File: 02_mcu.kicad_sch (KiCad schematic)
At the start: 31 parts, among them J2 0533980571, U3 MSPM0C1104SDDFR, U4 TLC59208F, U5 VEML7700, U6 TLV803E

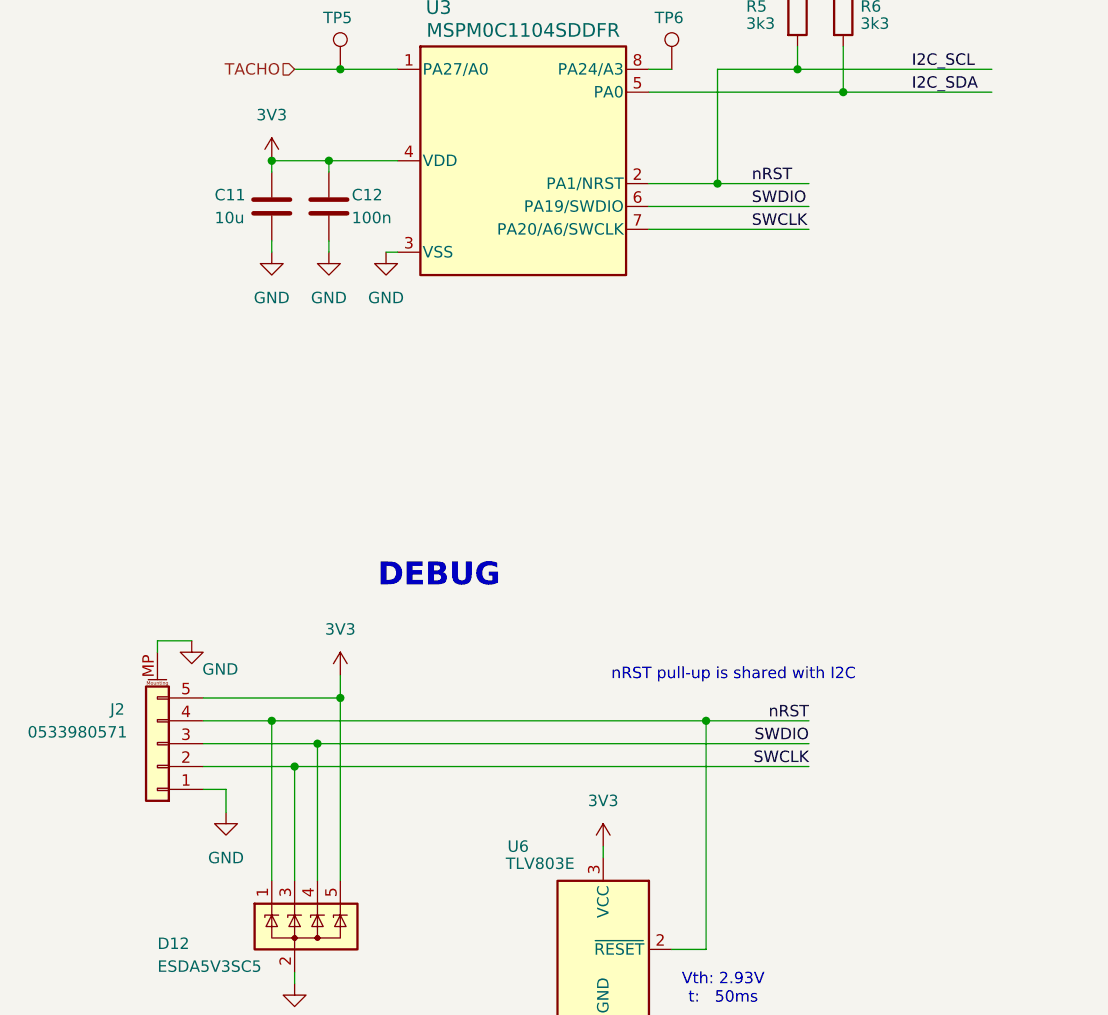
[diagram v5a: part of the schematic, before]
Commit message: Schematic: Remove nRST net label to avoid ERC warning
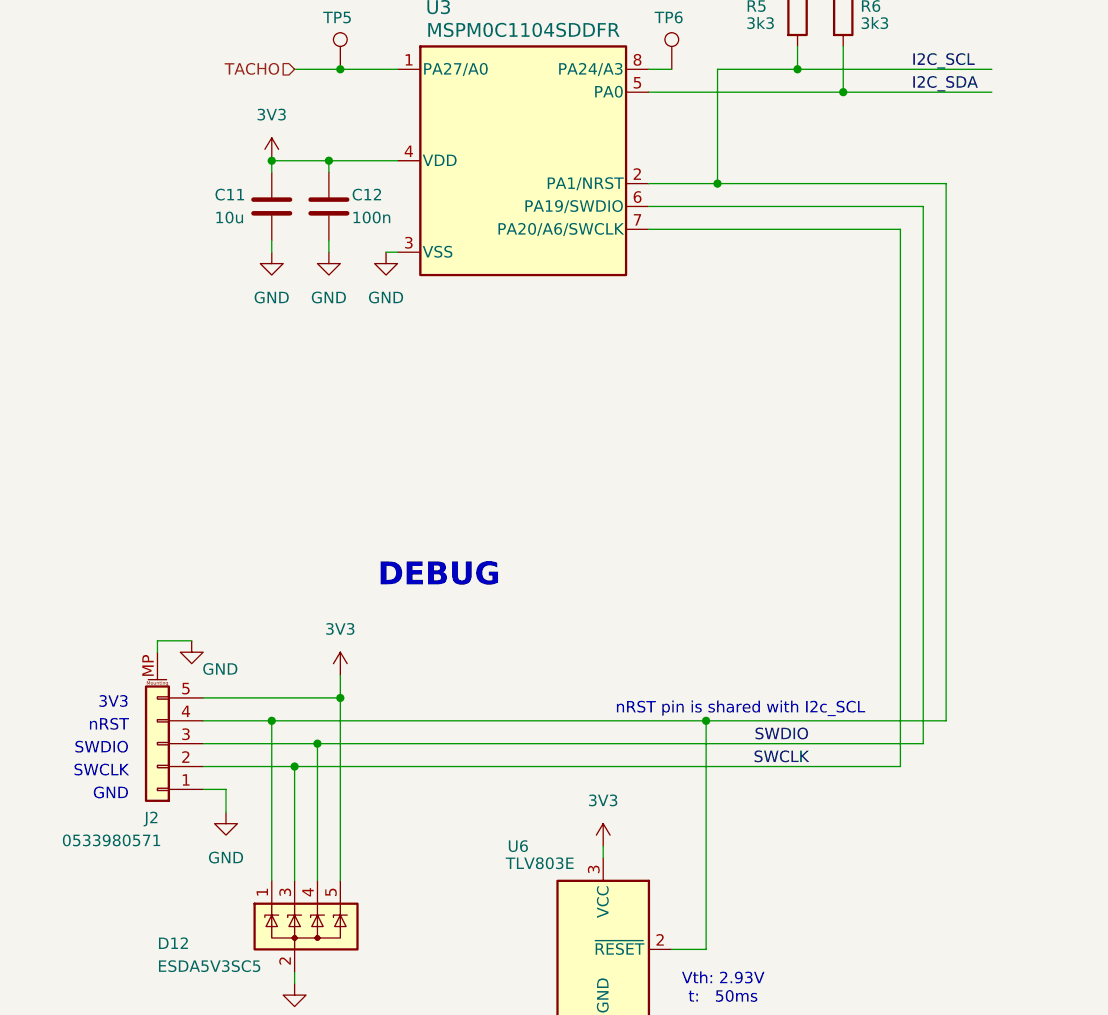
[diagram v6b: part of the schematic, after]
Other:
- note added: "3V3"
- note added: "GND"
- note added: "SWCLK"
- note added: "SWDIO"
- note added: "nRST"
- note added: "nRST pin is shared with I2c_SCL"
- note removed: "nRST pull-up is shared with I2C"
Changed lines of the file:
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@@
 	(wire
 		(pts
-			(xy 50.8 132.08) (xy 105.41 132.08)
+			(xy 50.8 132.08) (xy 118.11 132.08)
 		)
 		(stroke
@@
 	(wire
 		(pts
+			(xy 118.11 72.39) (xy 118.11 132.08)
+		)
+		(stroke
+			(width 0)
+			(type default)
+		)
+	)
+	(wire
+		(pts
 			(xy 213.36 85.09) (xy 213.36 92.71)
 		)
@@
 	(wire
 		(pts
-			(xy 87.63 74.93) (xy 105.41 74.93)
+			(xy 87.63 74.93) (xy 115.57 74.93)
 		)
 		(stroke
@@
 	(wire
 		(pts
-			(xy 48.26 134.62) (xy 105.41 134.62)
+			(xy 48.26 134.62) (xy 115.57 134.62)
 		)
 		(stroke
@@
 	(wire
 		(pts
+			(xy 115.57 74.93) (xy 115.57 134.62)
+		)
+		(stroke
+			(width 0)
+			(type default)
+		)
+	)
+	(wire
+		(pts
 			(xy 87.63 57.15) (xy 90.17 57.15)
 		)
@@
 	(wire
 		(pts
-			(xy 95.25 69.85) (xy 105.41 69.85)
+			(xy 95.25 69.85) (xy 120.65 69.85)
 		)
 		(stroke
@@
 	(wire
 		(pts
-			(xy 93.98 129.54) (xy 105.41 129.54)
+			(xy 93.98 129.54) (xy 120.65 129.54)
 		)
 		(stroke
@@
 	(wire
 		(pts
+			(xy 120.65 69.85) (xy 120.65 129.54)
+		)
+		(stroke
+			(width 0)
+			(type default)
+		)
+	)
+	(wire
+		(pts
 			(xy 181.61 87.63) (xy 181.61 90.17)
 		)
@@
 	(wire
 		(pts
-			(xy 87.63 72.39) (xy 105.41 72.39)
+			(xy 87.63 72.39) (xy 118.11 72.39)
 		)
 		(stroke
@@
 		)
 	)
+	(text "nRST"
+		(exclude_from_sim no)
+		(at 29.845 130.175 0)
+		(effects
+			(font
+				(size 1.27 1.27)
+			)
+			(justify right)
+		)
+	)
 	(text "MCU"
 		(exclude_from_sim no)
@@
 		)
 	)
-	(text "nRST pull-up is shared with I2C"
-		(exclude_from_sim no)
-		(at 97.028 124.46 0)
+	(text "SWCLK"
+		(exclude_from_sim no)
+		(at 29.845 135.255 0)
 		(effects
 			(font
 				(size 1.27 1.27)
 			)
+			(justify right)
+		)
+	)
+	(text "3V3"
+		(exclude_from_sim no)
+		(at 29.845 127.635 0)
+		(effects
+			(font
+				(size 1.27 1.27)
+			)
+			(justify right)
+		)
+	)
+	(text "nRST pin is shared with I2c_SCL"
+		(exclude_from_sim no)
+		(at 97.79 128.27 0)
+		(effects
+			(font
+				(size 1.27 1.27)
+			)
+		)
+	)
+	(text "GND"
+		(exclude_from_sim no)
+		(at 29.845 137.795 0)
+		(effects
+			(font
+				(size 1.27 1.27)
+			)
+			(justify right)
 		)
 	)
@@
 		)
 	)
+	(text "SWDIO"
+		(exclude_from_sim no)
+		(at 29.845 132.715 0)
+		(effects
+			(font
+				(size 1.27 1.27)
+			)
+			(justify right)
+		)
+	)
 	(text "DEBUG"
 		(exclude_from_sim no)
@@
 		)
 	)
-	(label "SWCLK"
-		(at 99.06 74.93 0)
-		(fields_autoplaced yes)
-		(effects
-			(font
-				(size 1.27 1.27)
-			)
-			(justify left bottom)
-		)
-	)
 	(label "I2C_SCL"
 		(at 116.84 57.15 0)
@@
 		)
 	)
-	(label "nRST"
-		(at 99.06 69.85 0)
-		(fields_autoplaced yes)
-		(effects
-			(font
-				(size 1.27 1.27)
-			)
-			(justify left bottom)
-		)
-	)
 	(label "I2C_SDA"
 		(at 176.53 152.4 0)
@@
 	)
 	(label "SWDIO"
-		(at 99.06 72.39 0)
-		(fields_autoplaced yes)
-		(effects
-			(font
-				(size 1.27 1.27)
-			)
-			(justify left bottom)
-		)
-	)
-	(label "SWDIO"
 		(at 105.41 132.08 180)
 		(fields_autoplaced yes)
@@
 	(label "SWCLK"
 		(at 105.41 134.62 180)
-		(fields_autoplaced yes)
-		(effects
-			(font
-				(size 1.27 1.27)
-			)
-			(justify right bottom)
-		)
-	)
-	(label "nRST"
-		(at 105.41 129.54 180)
 		(fields_autoplaced yes)
 		(effects
@@
 		(dnp no)
 		(property "Reference" "J2"
-			(at 28.575 128.27 0)
+			(at 32.385 140.335 0)
 			(effects
 				(font
@@
 		)
 		(property "Value" "0533980571"
-			(at 24.13 130.81 0)
-			(effects
-				(font
+			(at 27.94 142.875 0)
+			(effects
+				(font

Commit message: Ci: Fill title header in generated schematic
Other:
- title: (none) -> ${PROJECTNAME}
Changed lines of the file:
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@@
 	(generator_version "8.0")
 	(paper "A4")
+	(title_block
+		(title "${PROJECTNAME}")
+		(date "${ISSUE_DATE}")
+		(rev "${REVISION}")
+	)
 	(junction
 		(at 106.68 45.72)

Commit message: Schematic: Remove Testpoints from BOM
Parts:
- TP5, TP6: now left out of the parts list
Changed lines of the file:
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@@
 		(unit 1)
 		(exclude_from_sim no)
-		(in_bom yes)
+		(in_bom no)
 		(on_board yes)
 		(dnp no)
@@
 		(unit 1)
 		(exclude_from_sim no)
-		(in_bom yes)
-		(on_board yes)
-		(dnp no)
+		(in_bom no)
+		(on_board yes)
+		(dnp no)
